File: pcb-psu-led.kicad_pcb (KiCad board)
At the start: 2 copper layers, 140 x 80 mm, 16 parts, among them J1 MAINS INPUT 230V, J2 LED PANEL OUT JST XH, T1 Talema 70000K, U1 LM78L05ACZ

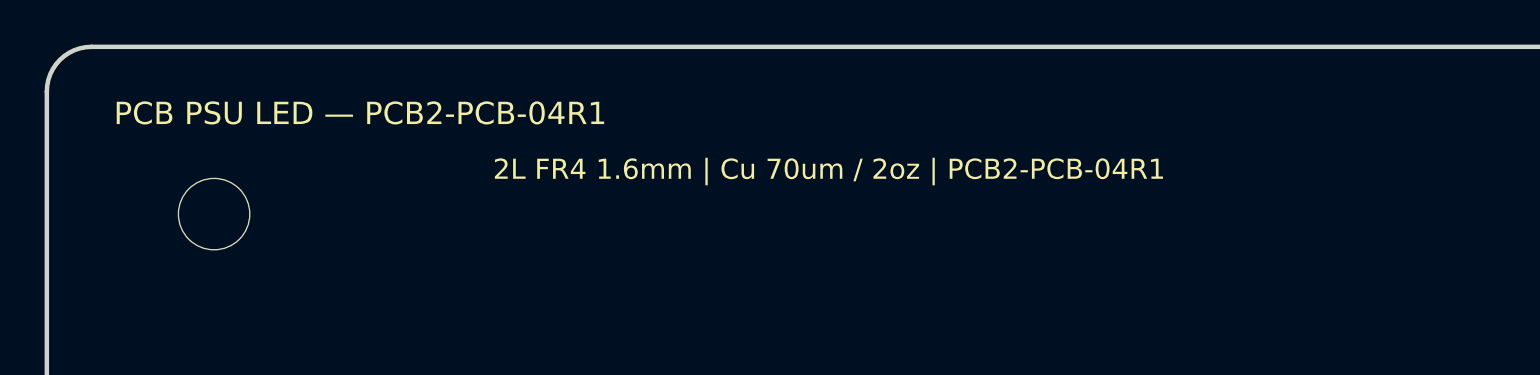
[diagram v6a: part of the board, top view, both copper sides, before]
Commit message: PCB2-PCB-04R2: change production copper to 1 oz
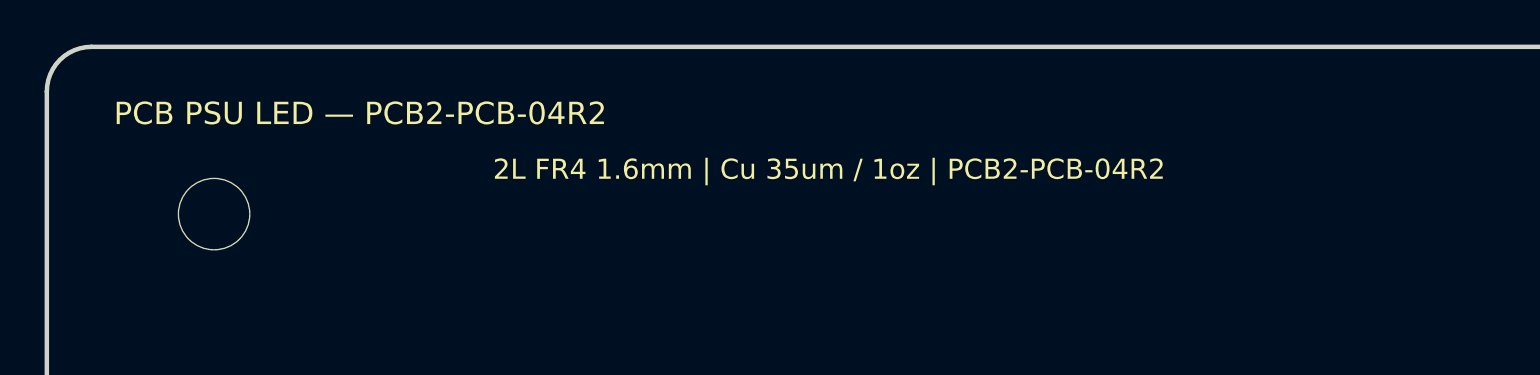
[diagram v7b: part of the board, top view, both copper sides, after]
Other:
- board text added: "2L FR4 1.6mm | Cu 35um / 1oz | PCB2-PCB-04R2"
- board text added: "PCB PSU LED — PCB2-PCB-04R2"
- board text removed: "2L FR4 1.6mm | Cu 70um / 2oz | PCB2-PCB-04R1"
- board text removed: "PCB PSU LED — PCB2-PCB-04R1"
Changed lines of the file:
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@@
     (title "PCB PSU LED")
     (date "2026-07-16")
-    (rev "PCB2-PCB-04R1")
+    (rev "PCB2-PCB-04R2")
     (company "Custom Step-Down PSU 230 V to 100 V")
-    (comment 1 "Production marking review: connector polarity and revision identification")
+    (comment 1 "Production stackup: FR4 1.6 mm, Cu 35 um / 1 oz")
   )
   (layers
@@
       (layer "F.Paste" (type "Top Solder Paste"))
       (layer "F.Mask" (type "Top Solder Mask") (color "Green") (thickness 0.01))
-      (layer "F.Cu" (type "copper") (thickness 0.07))
-      (layer "dielectric 1" (type "core") (thickness 1.46) (material "FR4") (epsilon_r 4.5) (loss_tangent 0.02))
-      (layer "B.Cu" (type "copper") (thickness 0.07))
+      (layer "F.Cu" (type "copper") (thickness 0.035))
+      (layer "dielectric 1" (type "core") (thickness 1.51) (material "FR4") (epsilon_r 4.5) (loss_tangent 0.02))
+      (layer "B.Cu" (type "copper") (thickness 0.035))
       (layer "B.Mask" (type "Bottom Solder Mask") (color "Green") (thickness 0.01))
       (layer "B.Paste" (type "Bottom Solder Paste"))
@@
   (gr_line (start 0 78) (end 0 2) (stroke (width 0.2) (type default)) (layer "Edge.Cuts"))
   (gr_arc (start 0 2) (mid 0.5858 0.5858) (end 2 0) (stroke (width 0.2) (type default)) (layer "Edge.Cuts"))
-  (gr_text "PCB PSU LED — PCB2-PCB-04R1" (at 3 3) (layer "F.SilkS")
+  (gr_text "PCB PSU LED — PCB2-PCB-04R2" (at 3 3) (layer "F.SilkS")
     (effects (font (size 1 1) (thickness 0.15)) (justify left))
   )
-  (gr_text "2L FR4 1.6mm | Cu 70um / 2oz | PCB2-PCB-04R1" (at 20 5.5) (layer "F.SilkS")
+  (gr_text "2L FR4 1.6mm | Cu 35um / 1oz | PCB2-PCB-04R2" (at 20 5.5) (layer "F.SilkS")
     (effects (font (size 0.9 0.9) (thickness 0.12)) (justify left))
   )
